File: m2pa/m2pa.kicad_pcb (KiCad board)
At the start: 2 copper layers, 47 x 28 mm, 23 parts, among them IC1 ADL5324, M3_MOUNT VAL**, P1 CONN_01X02, P2 SMA, P3 SMA

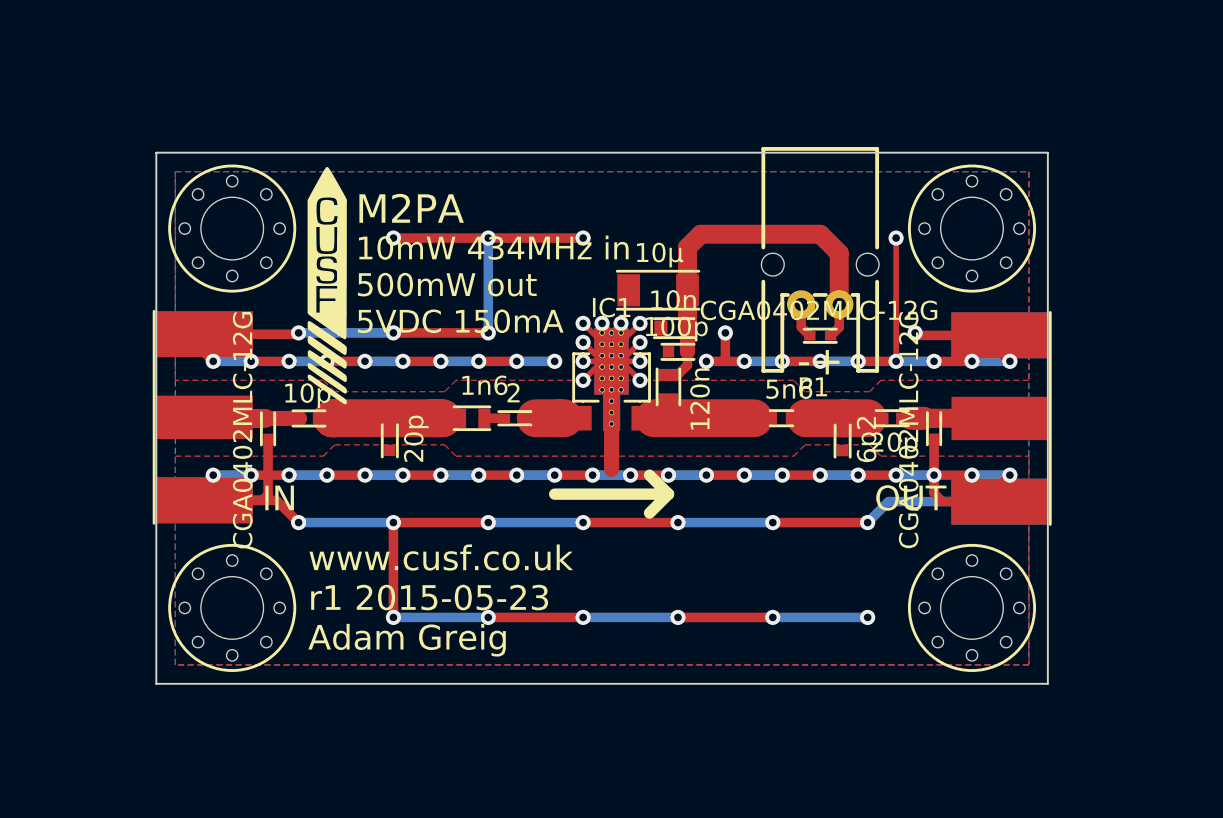
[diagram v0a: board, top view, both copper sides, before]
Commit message: make case-size version of M2PA
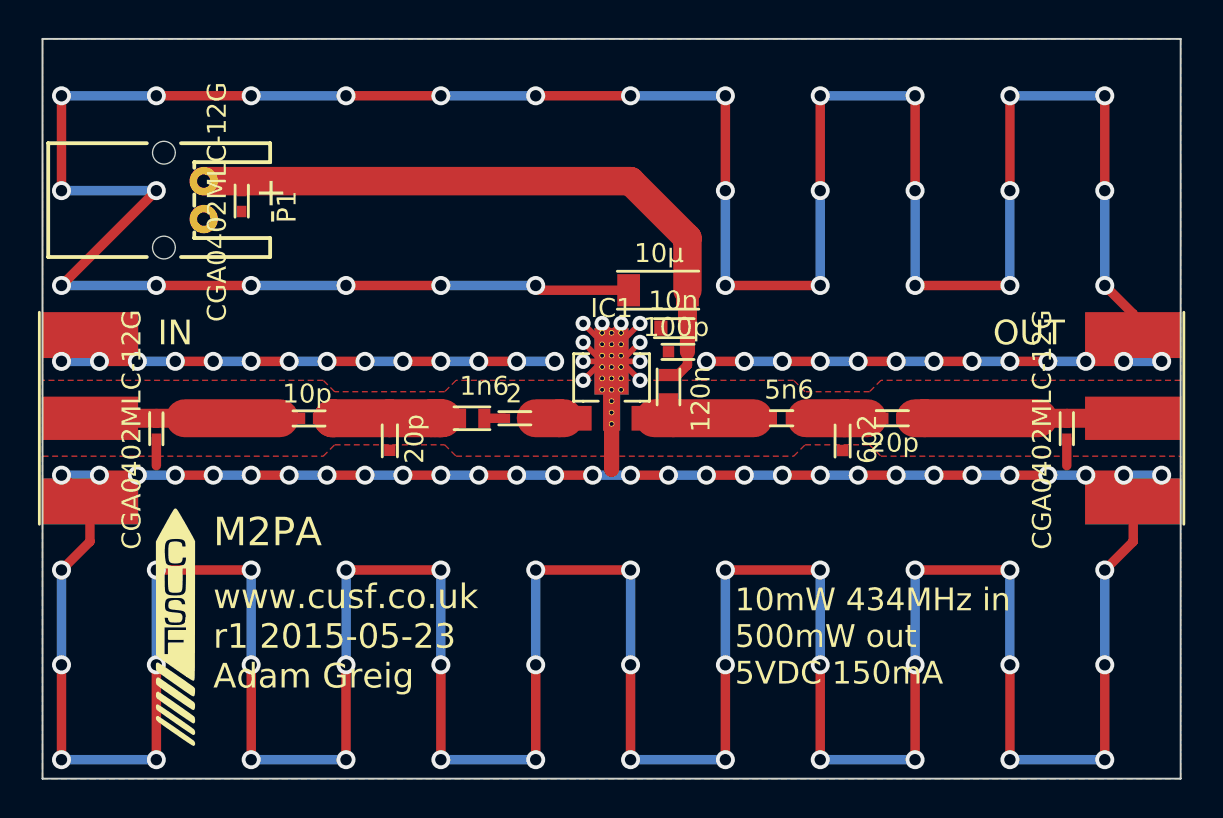
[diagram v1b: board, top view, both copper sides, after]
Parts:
- removed M3_MOUNT (x4): VAL**, m2pa:M3_MOUNT
- added G***: LOGO, m2pa:cusf_logo_full, F.Cu at (140.5, 87.5)
- moved D3 32.0 mm to (119.5, 75.0), turned to 270 degrees
- moved P1 31.8 mm to (117.5, 76.5), turned to 90 degrees
- moved G*** 19.7 mm to (116.0, 98.0)
- moved P3 7.04 mm to (166.5, 87.0)
- moved D2 7.00 mm to (163.0, 87.0)
- moved P2 6.05 mm to (111.5, 87.0)
- moved D1 5.89 mm to (115.0, 87.0)
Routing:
- net GND: track 235.4 -> 478.8 mm, vias 73 -> 133
- net +5V: track 20.7 -> 35.2 mm
- net Net-(C7-Pad2): track 5.16 -> 12.2 mm
- net Net-(C1-Pad2): track 5.23 -> 11.1 mm
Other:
- board size 47 x 28 mm -> 60 x 39 mm
